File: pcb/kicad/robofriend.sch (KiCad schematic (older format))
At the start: 127 parts, among them J1 PWR, J10 US3, J11 US4, J12 I2C, J13 I2C, J14 I2C, J15 I2C, J16 12V-Buck, J17 5VIN, J18 5VOUT, J19 5VOUT, J20 USB_A_4_PIN, J21 MON/AMP, J22 ADC1, J23 MRi, J24 SPI, J25 ADC2, J26 MLe, J27 M1, J28 M2, J29 IR1, J30 IR2, J31 UART, J32 IR3, J33 GS2, J4 PWR, J5 US1, J6 3V3OUT, J7 3V3OUT, J8 GS2, J9 US2, K1 SCHRACK-RTx3, Q1 NMOS, Q2 NMOS, Q3 NMOS, Q4 NPN, Q5 PMOS, Q6 NMOS, Q7 NMOS, U1 LM3940-3.3, U2 Teensy++2.0, U3 TL331, U4 LM4040, U5 MCP6001, U6 INA193, U7 TL331, U8 TXS0102

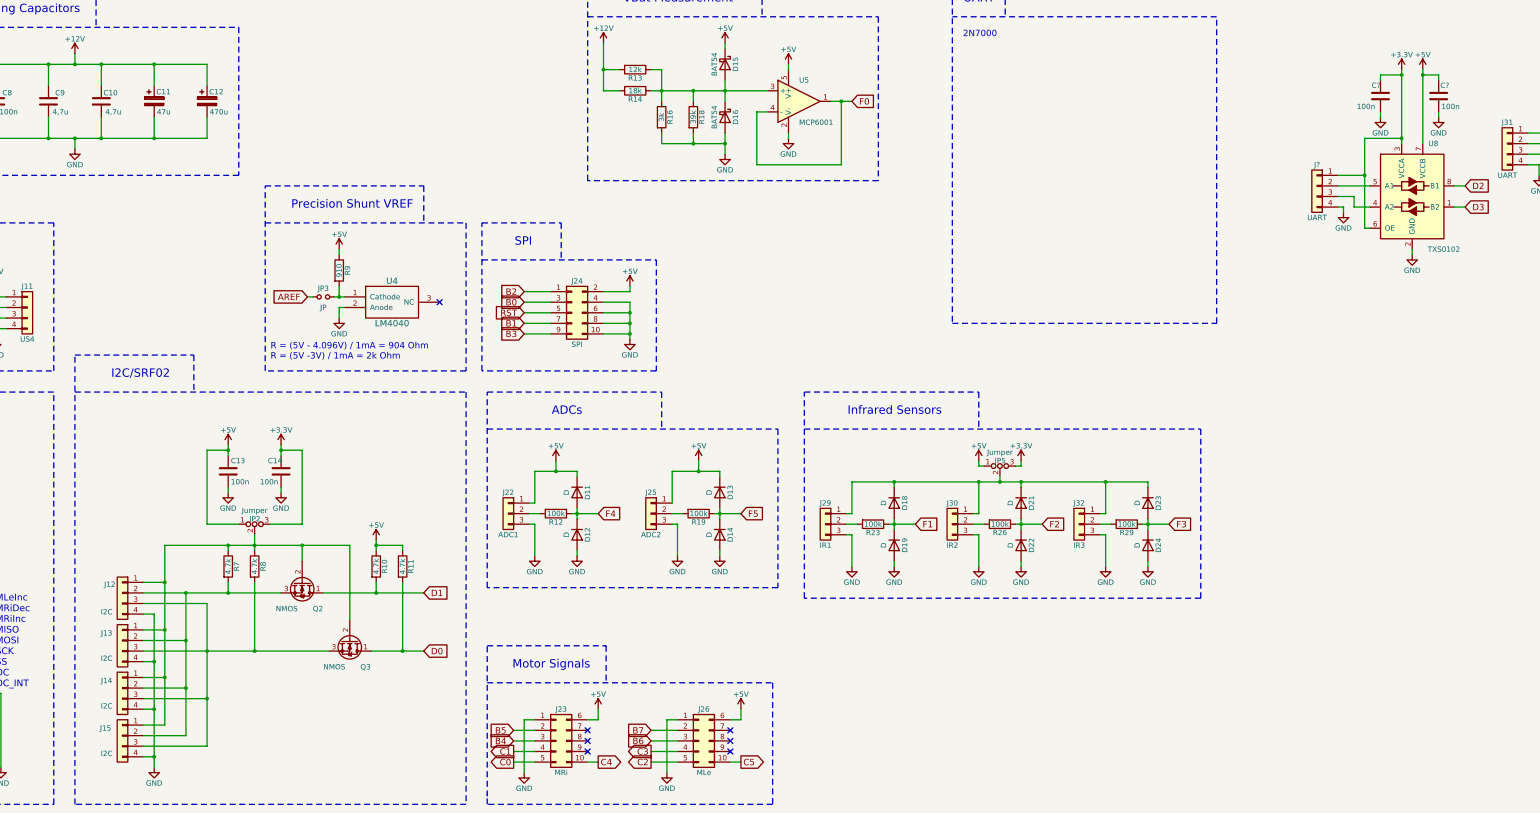
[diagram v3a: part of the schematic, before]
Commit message: removed 100n capacitors for i2c interface
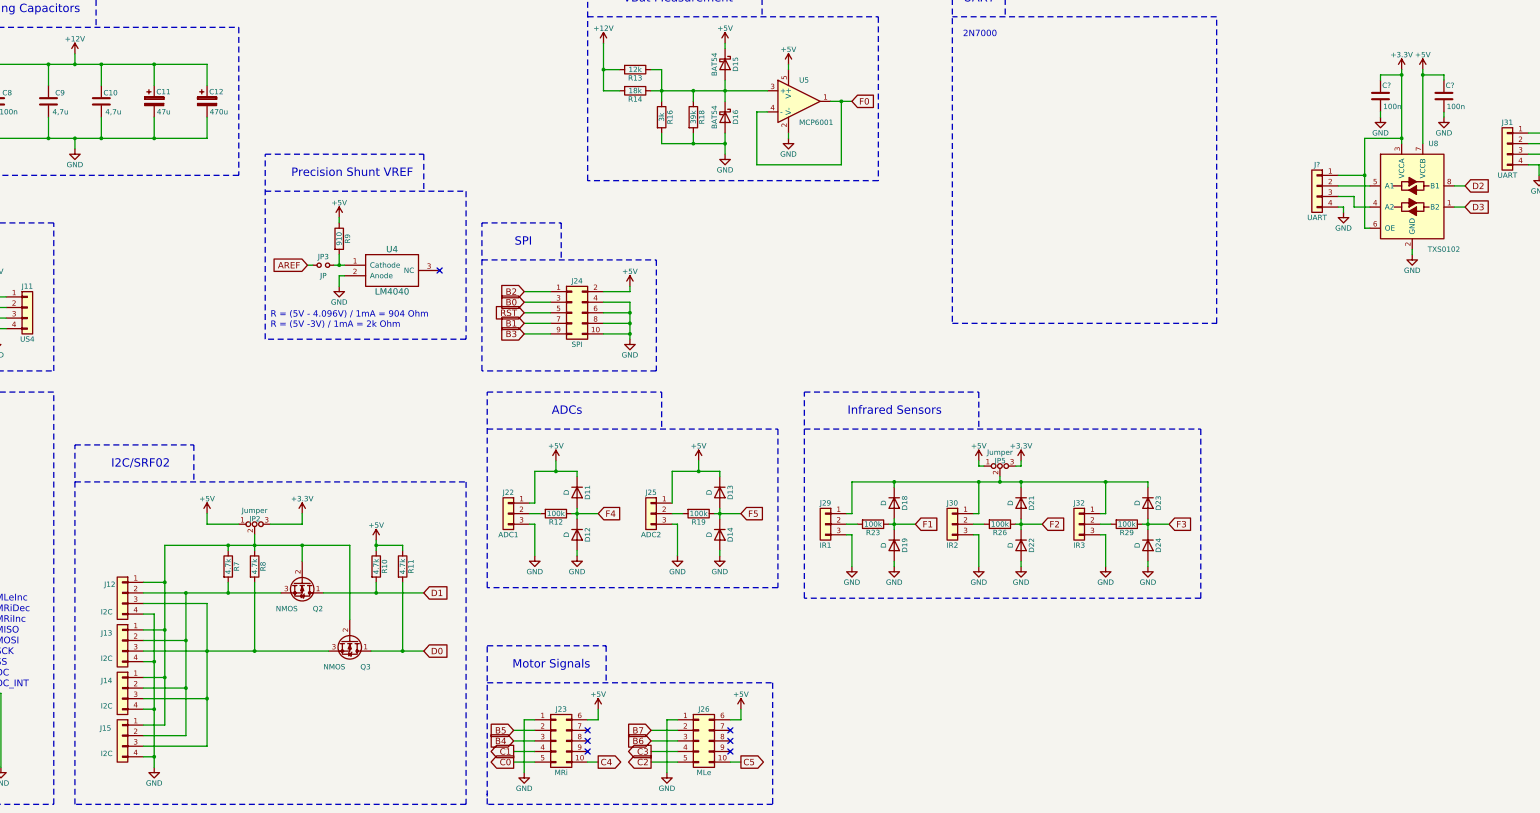
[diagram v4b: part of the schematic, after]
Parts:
- removed C13, C14: 100n, Capacitors_SMD:C_0603, symbol C
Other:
- moved on the sheet: C?, JP3, R9, U4
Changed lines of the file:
@@
 L LM4040 U4
 U 1 1 5B0810EB
-P 8000 6750
-F 0 "U4" H 8000 6950 60  0000 C CNN
-F 1 "LM4040" H 8000 6550 60  0000 C CNN
-F 2 "TO_SOT_Packages_SMD:SOT-23" H 7850 6700 60  0001 C CNN
-F 3 "" H 7850 6700 60  0001 C CNN
-	1    8000 6750
+P 8000 6450
+F 0 "U4" H 8000 6650 60  0000 C CNN
+F 1 "LM4040" H 8000 6250 60  0000 C CNN
+F 2 "TO_SOT_Packages_SMD:SOT-23" H 7850 6400 60  0001 C CNN
+F 3 "" H 7850 6400 60  0001 C CNN
+	1    8000 6450
 	1    0    0    -1
 $EndComp
@@
 L R R9
 U 1 1 5B081351
-P 7500 6450
-F 0 "R9" V 7580 6450 50  0000 C CNN
-F 1 "910" V 7500 6450 50  0000 C CNN
-F 2 "Resistors_SMD:R_0603" V 7430 6450 50  0001 C CNN
-F 3 "" H 7500 6450 50  0001 C CNN
-	1    7500 6450
+P 7500 6150
+F 0 "R9" V 7580 6150 50  0000 C CNN
+F 1 "910" V 7500 6150 50  0000 C CNN
+F 2 "Resistors_SMD:R_0603" V 7430 6150 50  0001 C CNN
+F 3 "" H 7500 6150 50  0001 C CNN
+	1    7500 6150
 	1    0    0    -1
 $EndComp
@@
 L +5V #PWR030
 U 1 1 5B0814E4
-P 7500 6250
-F 0 "#PWR030" H 7500 6100 50  0001 C CNN
-F 1 "+5V" H 7500 6390 50  0000 C CNN
-F 2 "" H 7500 6250 50  0001 C CNN
-F 3 "" H 7500 6250 50  0001 C CNN
-	1    7500 6250
+P 7500 5950
+F 0 "#PWR030" H 7500 5800 50  0001 C CNN
+F 1 "+5V" H 7500 6090 50  0000 C CNN
+F 2 "" H 7500 5950 50  0001 C CNN
+F 3 "" H 7500 5950 50  0001 C CNN
+	1    7500 5950
 	1    0    0    -1
 $EndComp
@@
 L GND #PWR031
 U 1 1 5B081963
-P 7500 6900
-F 0 "#PWR031" H 7500 6650 50  0001 C CNN
-F 1 "GND" H 7500 6750 50  0000 C CNN
-F 2 "" H 7500 6900 50  0001 C CNN
-F 3 "" H 7500 6900 50  0001 C CNN
-	1    7500 6900
+P 7500 6600
+F 0 "#PWR031" H 7500 6350 50  0001 C CNN
+F 1 "GND" H 7500 6450 50  0000 C CNN
+F 2 "" H 7500 6600 50  0001 C CNN
+F 3 "" H 7500 6600 50  0001 C CNN
+	1    7500 6600
 	1    0    0    -1
 $EndComp
-Text Notes 6850 7300 0    60   ~ 0
+Text Notes 6850 7000 0    60   ~ 0
 R = (5V - 4.096V) / 1mA = 904 Ohm\nR = (5V -3V) / 1mA = 2k Ohm
-NoConn ~ 8450 6750
+NoConn ~ 8450 6450
 $Comp
 L Q_NMOS_DGS Q1
@@
 Text GLabel 3900 11050 2    60   Input ~ 0
 F4
-Text GLabel 7200 6700 0    60   Input ~ 0
+Text GLabel 7200 6400 0    60   Input ~ 0
 AREF
 Text GLabel 9950 8750 2    60   Input ~ 0
@@
 Text Notes 13700 3925 2    79   ~ 0
 UART
-Text Notes 5900 7475 2    79   ~ 0
+Text Notes 5900 8325 2    79   ~ 0
 I2C/SRF02
-Text Notes 8200 5875 2    79   ~ 0
+Text Notes 8200 5575 2    79   ~ 0
 Precision Shunt VREF
 Text Notes 1650 7475 2    79   ~ 0
@@
 $EndComp
 $Comp
-L C C13
-U 1 1 5B3C6772
-P 6450 8350
-F 0 "C13" H 6475 8450 50  0000 L CNN
-F 1 "100n" H 6475 8250 50  0000 L CNN
-F 2 "Capacitors_SMD:C_0603" H 6488 8200 50  0001 C CNN
-F 3 "" H 6450 8350 50  0001 C CNN
-	1    6450 8350
-	1    0    0    -1
-$EndComp
-$Comp
-L GND #PWR064
-U 1 1 5B3C6778
-P 6450 8550
-F 0 "#PWR064" H 6450 8300 50  0001 C CNN
-F 1 "GND" H 6450 8400 50  0000 C CNN
-F 2 "" H 6450 8550 50  0001 C CNN
-F 3 "" H 6450 8550 50  0001 C CNN
-	1    6450 8550
-	1    0    0    -1
-$EndComp
-$Comp
 L +3.3V #PWR065
 U 1 1 5B3C677E
-P 6950 8100
-F 0 "#PWR065" H 6950 7950 50  0001 C CNN
-F 1 "+3.3V" H 6950 8240 50  0000 C CNN
-F 2 "" H 6950 8100 50  0001 C CNN
-F 3 "" H 6950 8100 50  0001 C CNN
-	1    6950 8100
+P 7150 8750
+F 0 "#PWR065" H 7150 8600 50  0001 C CNN
+F 1 "+3.3V" H 7150 8890 50  0000 C CNN
+F 2 "" H 7150 8750 50  0001 C CNN
+F 3 "" H 7150 8750 50  0001 C CNN
+	1    7150 8750
 	1    0    0    -1
 $EndComp
@@
 L +5V #PWR066
 U 1 1 5B3C6784
-P 6450 8100
-F 0 "#PWR066" H 6450 7950 50  0001 C CNN
-F 1 "+5V" H 6450 8240 50  0000 C CNN
-F 2 "" H 6450 8100 50  0001 C CNN
-F 3 "" H 6450 8100 50  0001 C CNN
-	1    6450 8100
-	1    0    0    -1
-$EndComp
-$Comp
-L C C14
-U 1 1 5B3C678A
-P 6950 8350
-F 0 "C14" H 6825 8450 50  0000 L CNN
-F 1 "100n" H 6750 8250 50  0000 L CNN
-F 2 "Capacitors_SMD:C_0603" H 6988 8200 50  0001 C CNN
-F 3 "" H 6950 8350 50  0001 C CNN
-	1    6950 8350
-	1    0    0    -1
-$EndComp
-$Comp
-L GND #PWR067
-U 1 1 5B3C6790
-P 6950 8550
-F 0 "#PWR067" H 6950 8300 50  0001 C CNN
-F 1 "GND" H 6950 8400 50  0000 C CNN
-F 2 "" H 6950 8550 50  0001 C CNN
-F 3 "" H 6950 8550 50  0001 C CNN
-	1    6950 8550
+P 6250 8750
+F 0 "#PWR066" H 6250 8600 50  0001 C CNN
+F 1 "+5V" H 6250 8890 50  0000 C CNN
+F 2 "" H 6250 8750 50  0001 C CNN
+F 3 "" H 6250 8750 50  0001 C CNN
+	1    6250 8750
 	1    0    0    -1
 $EndComp
@@
 L Jumper_NO_Small JP3
 U 1 1 5B47AB1D
-P 7350 6700
-F 0 "JP3" H 7350 6780 50  0000 C CNN
-F 1 "JP" H 7350 6600 50  0000 C CNN
-F 2 "Pin_Headers:Pin_Header_Straight_1x02_Pitch2.54mm" H 7350 6700 50  0001 C CNN
-F 3 "" H 7350 6700 50  0001 C CNN
-	1    7350 6700
+P 7350 6400
+F 0 "JP3" H 7350 6480 50  0000 C CNN
+F 1 "JP" H 7350 6300 50  0000 C CNN
+F 2 "Pin_Headers:Pin_Header_Straight_1x02_Pitch2.54mm" H 7350 6400 50  0001 C CNN
+F 3 "" H 7350 6400 50  0001 C CNN
+	1    7350 6400
 	1    0    0    -1
 $EndComp
@@
 Wire Wire Line
 	10550 4750 10550 4850
-Connection ~ 7500 6700
+Connection ~ 7500 6400
 Wire Wire Line
-	7500 6800 7500 6900
+	7500 6500 7500 6600
 Wire Wire Line
-	7550 6800 7500 6800
+	7550 6500 7500 6500
 Wire Wire Line
-	7450 6700 7500 6700
+	7450 6400 7500 6400
 Wire Wire Line
-	7500 6700 7550 6700
+	7500 6400 7550 6400
 Wire Wire Line
-	7500 6600 7500 6700
+	7500 6300 7500 6400
 Wire Wire Line
-	7500 6300 7500 6250
+	7500 6000 7500 5950
 Wire Wire Line
 	5850 9050 5850 9400
@@
 	15150 8450 15150 8500
 Wire Wire Line
-	14700 8750 14750 8750
+	14750 8750 14700 8750
 Wire Wire Line
 	9300 8650 9350 8650
@@
 	13300 3700 13300 6950
 Wire Notes Line
-	5000 7600 8700 7600
+	5000 8450 8700 8450
 Wire Notes Line
-	8700 7600 8700 11500
+	8700 8450 8700 11500
 Wire Notes Line
 	8700 11500 5000 11500
@@
 	13800 3700 13800 4050
 Wire Notes Line
-	6125 7250 6125 7600
+	6125 8100 6125 8450
 Wire Notes Line
-	5000 7250 6125 7250
+	5000 8100 6125 8100
 Wire Notes Line
-	5000 11500 5000 7250
+	5000 11500 5000 8100
 Wire Notes Line
-	6800 6000 8700 6000
+	6800 5700 8700 5700
 Wire Notes Line
-	8300 5650 8300 6000
+	8300 5350 8300 5700
 Wire Notes Line
-	6800 5650 8300 5650
+	6800 5350 8300 5350
 Wire Notes Line
-	6800 7400 6800 5650
+	6800 7100 6800 5350
 Wire Notes Line
-	8700 6000 8700 7400
+	8700 5700 8700 7100
 Wire Notes Line
-	8700 7400 6800 7400
+	8700 7100 6800 7100
 Wire Notes Line
 	4800 11500 4800 7600
@@
 	6700 9050 6700 9100
 Wire Wire Line
-	6950 8500 6950 8550
-Connection ~ 6950 8150
-Wire Wire Line
-	7150 8850 6850 8850
-Wire Wire Line
-	7150 8150 7150 8850
-Wire Wire Line
-	6950 8150 7150 8150
-Wire Wire Line
-	6950 8100 6950 8150
-Wire Wire Line
-	6950 8150 6950 8200
-Wire Wire Line
-	6450 8500 6450 8550
-Connection ~ 6450 8150
-Wire Wire Line
-	6250 8850 6550 8850
-Wire Wire Line
-	6250 8150 6250 8850
-Wire Wire Line
-	6450 8150 6250 8150
-Wire Wire Line
-	6450 8100 6450 8150
-Wire Wire Line
-	6450 8150 6450 8200
-Wire Wire Line
 	7350 9500 7850 9500
 Wire Wire Line
@@
 	10850 5250 11150 5250
 Wire Wire Line
-	7250 6700 7200 6700
+	7250 6400 7200 6400
 Wire Wire Line
 	13600 2450 13600 2250
@@
 L C C?
 U 1 1 5B6F99CC
-P 17900 4800
-F 0 "C?" H 17800 4900 50  0000 L CNN
-F 1 "100n" H 17700 4700 50  0000 L CNN
-F 2 "Capacitors_SMD:C_0603" H 17938 4650 50  0001 C CNN
-F 3 "" H 17900 4800 50  0001 C CNN
-	1    17900 4800
+P 17950 4800
+F 0 "C?" H 17850 4900 50  0000 L CNN
+F 1 "100n" H 17750 4700 50  0000 L CNN
+F 2 "Capacitors_SMD:C_0603" H 17988 4650 50  0001 C CNN
+F 3 "" H 17950 4800 50  0001 C CNN
+	1    17950 4800
 	-1   0    0    -1
 $EndComp
@@
 L GND #PWR?
 U 1 1 5B6F99D2
-P 17900 5000
-F 0 "#PWR?" H 17900 4750 50  0001 C CNN
-F 1 "GND" H 17900 4850 50  0000 C CNN
-F 2 "" H 17900 5000 50  0001 C CNN
-F 3 "" H 17900 5000 50  0001 C CNN
-	1    17900 5000
+P 17950 5000
+F 0 "#PWR?" H 17950 4750 50  0001 C CNN
+F 1 "GND" H 17950 4850 50  0000 C CNN
+F 2 "" H 17950 5000 50  0001 C CNN
+F 3 "" H 17950 5000 50  0001 C CNN
+	1    17950 5000
 	-1   0    0    -1
 $EndComp
@@
 U 1 1 5B6F99E4
 P 17350 4800
-F 0 "C?" H 17350 4900 50  0000 L CNN
-F 1 "100n" H 17400 4700 50  0000 L CNN
+F 0 "C?" H 17250 4900 50  0000 L CNN
+F 1 "100n" H 17150 4700 50  0000 L CNN
 F 2 "Capacitors_SMD:C_0603" H 17388 4650 50  0001 C CNN
 F 3 "" H 17350 4800 50  0001 C CNN
@@
 	17350 4600 17550 4600
 Wire Wire Line
-	17900 4950 17900 5000
+	17950 4950 17950 5000
 Wire Wire Line
-	17900 4600 17750 4600
+	17950 4600 17750 4600
 Connection ~ 17750 4600
 Wire Wire Line
-	17900 4600 17900 4650
+	17950 4600 17950 4650
 Wire Wire Line
 	17350 4600 17350 4650
@@
 Connection ~ 12750 8450
 Connection ~ 13550 8450
+Wire Wire Line
+	6850 8850 7150 8850
+Wire Wire Line
+	7150 8850 7150 8750
+Wire Wire Line
+	6550 8850 6250 8850
+Wire Wire Line
+	6250 8850 6250 8750
 $EndSCHEMATC

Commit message: A3 size in schematic editor
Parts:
- gave numbers to parts that had none: 5
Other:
- moved on the sheet: C10, C11, C12, C2, C3, C7, C9, D18, D19, D21, D22, D23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

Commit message: layout almost done. the decision about the level shifters needs to be made
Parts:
- renumbered C17 to C13, C18 to C14, C19 to C15, C21 to C16, C24 to C17, C13 to C18, C14 to C19, D16 to D10, D17 to D11, D18 to D12, D19 to D13, D20 to D14, D21 to D15, D22 to D16, D23 to D17, D24 to D18, D11 to D5, D12 to D6, D13 to D7, D14 to D8, D15 to D9, J5 to J10, J16 to J11, J2 to J12, J17 to J13, J18 to J14, J19 to J15, J9 to J16, J10 to J17, J20 to J18, J11 to J19, J4 to J2, J3 to J20, J6 to J3, J7 to J4, J8 to J5, J12 to J6, J13 to J7, J14 to J8, J15 to J9, JP5 to JP4, JP6 to JP5

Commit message: added PCA9517 for i2c level shifting
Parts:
- removed JP5: Jumper, Pin_Headers:Pin_Header_Straight_1x03_Pitch2.54mm, symbol Jumper_NC_Dual
- removed Q2, Q3, Q6, Q7: NMOS, TO_SOT_Packages_SMD:SOT-23, symbol Q_NMOS_DGS
- removed R27, R28, R30, R31: 10k, Resistors_SMD:R_0603, symbol R
- added C? (x2): 100n, Capacitors_SMD:C_0603, symbol C
- added U?: PCA9517, symbol PCA9517
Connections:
- net +5V: now also J31.1 (Pin_1), C?.1, U?.5 (EN), U?.8 (VCCB)
- net D0: now also U?.6 (SDAB)
- net D1: now also U?.7 (SCLB)
- net D2: now also J31.2 (Pin_2)
- net D3: now also J31.3 (Pin_3)
- net GND: now also C?.2, C?.2, U?.4 (GND)
- net at J6.1 (Pin_1), J7.1 (Pin_1), J8.1 (Pin_1)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: now also C?.1, U?.1 (VCCA)
- net at J6.2 (Pin_2), J7.2 (Pin_2), J8.2 (Pin_2)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: now also U?.2 (SCLA)
- net at J6.3 (Pin_3), J7.3 (Pin_3), J8.3 (Pin_3)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: now also U?.3 (SDAA)
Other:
- note removed: "2N7000"
- moved on the sheet: C18, C19, D12, D13, D15, D16, D17, D18, D5, D6, D7, D8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

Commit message: schematic almost finished
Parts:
- removed C18, C19: 100n, Capacitors_SMD:C_0603, symbol C
- removed J34: UART, Pin_Headers:Pin_Header_Straight_1x04_Pitch2.54mm, symbol Conn_01x04
- removed U8: TXS0102, Housings_SSOP:SSOP-8_2.95x2.8mm_Pitch0.65mm, symbol TXB0102DCT
- U4: renamed from U?; footprint (none) -> Housings_SOIC:SOIC-8_3.9x4.9mm_Pitch1.27mm
- gave numbers to parts that had none: 2
- renumbered C13 to C15, C14 to C16, C15 to C17, C16 to C18, C17 to C19, D13 to D10, D5 to D11, D6 to D12, D15 to D13, D16 to D14, D7 to D15, D8 to D16, D9 to D5, D10 to D6, D11 to D7, D14 to D8, D12 to D9, J31 to J22, J26 to J25, J27 to J26, J28 to J27, J29 to J28, J22 to J29, J25 to J31, Q4 to Q2, Q5 to Q3, R13 to R12, R14 to R13, R15 to R14, R16 to R15, R17 to R16, R18 to R17, R20 to R18, R21 to R19, R22 to R20, R24 to R21, R25 to R22, R12 to R24, R26 to R25, R19 to R26, R29 to R27, U4 to U5, U5 to U6, U6 to U7, U7 to U8
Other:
- moved on the sheet: C1, C10, C11, C12, C15, C16, C17, C18, C19, C4, C5, C6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
